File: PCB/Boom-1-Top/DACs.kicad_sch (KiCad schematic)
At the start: 13 parts, among them J36 SPIBus1Test, J37 Osc1Conn, J38 Osc2Conn, U3 AD5290, U4 AD5290

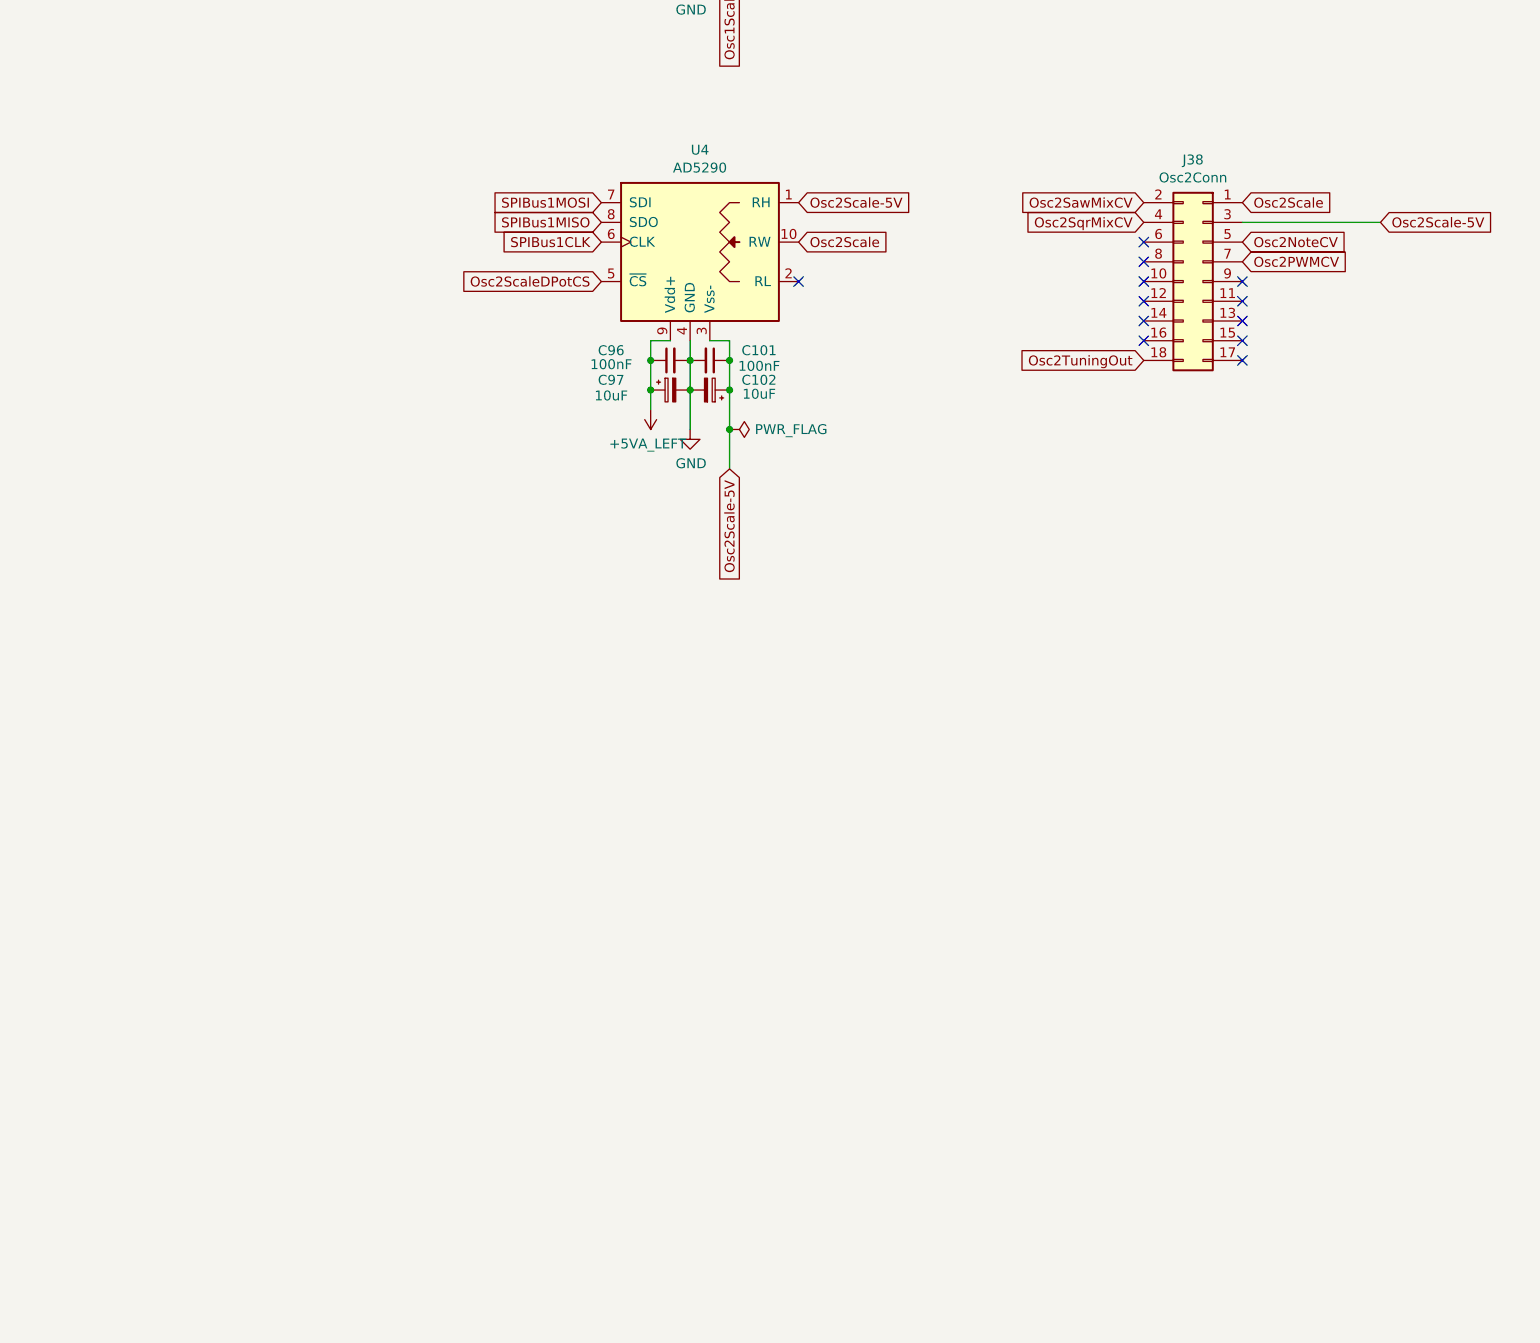
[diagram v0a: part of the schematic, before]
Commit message: Top: moved power connectors to Power Rails; moved anything pertaining to DACs into DACs
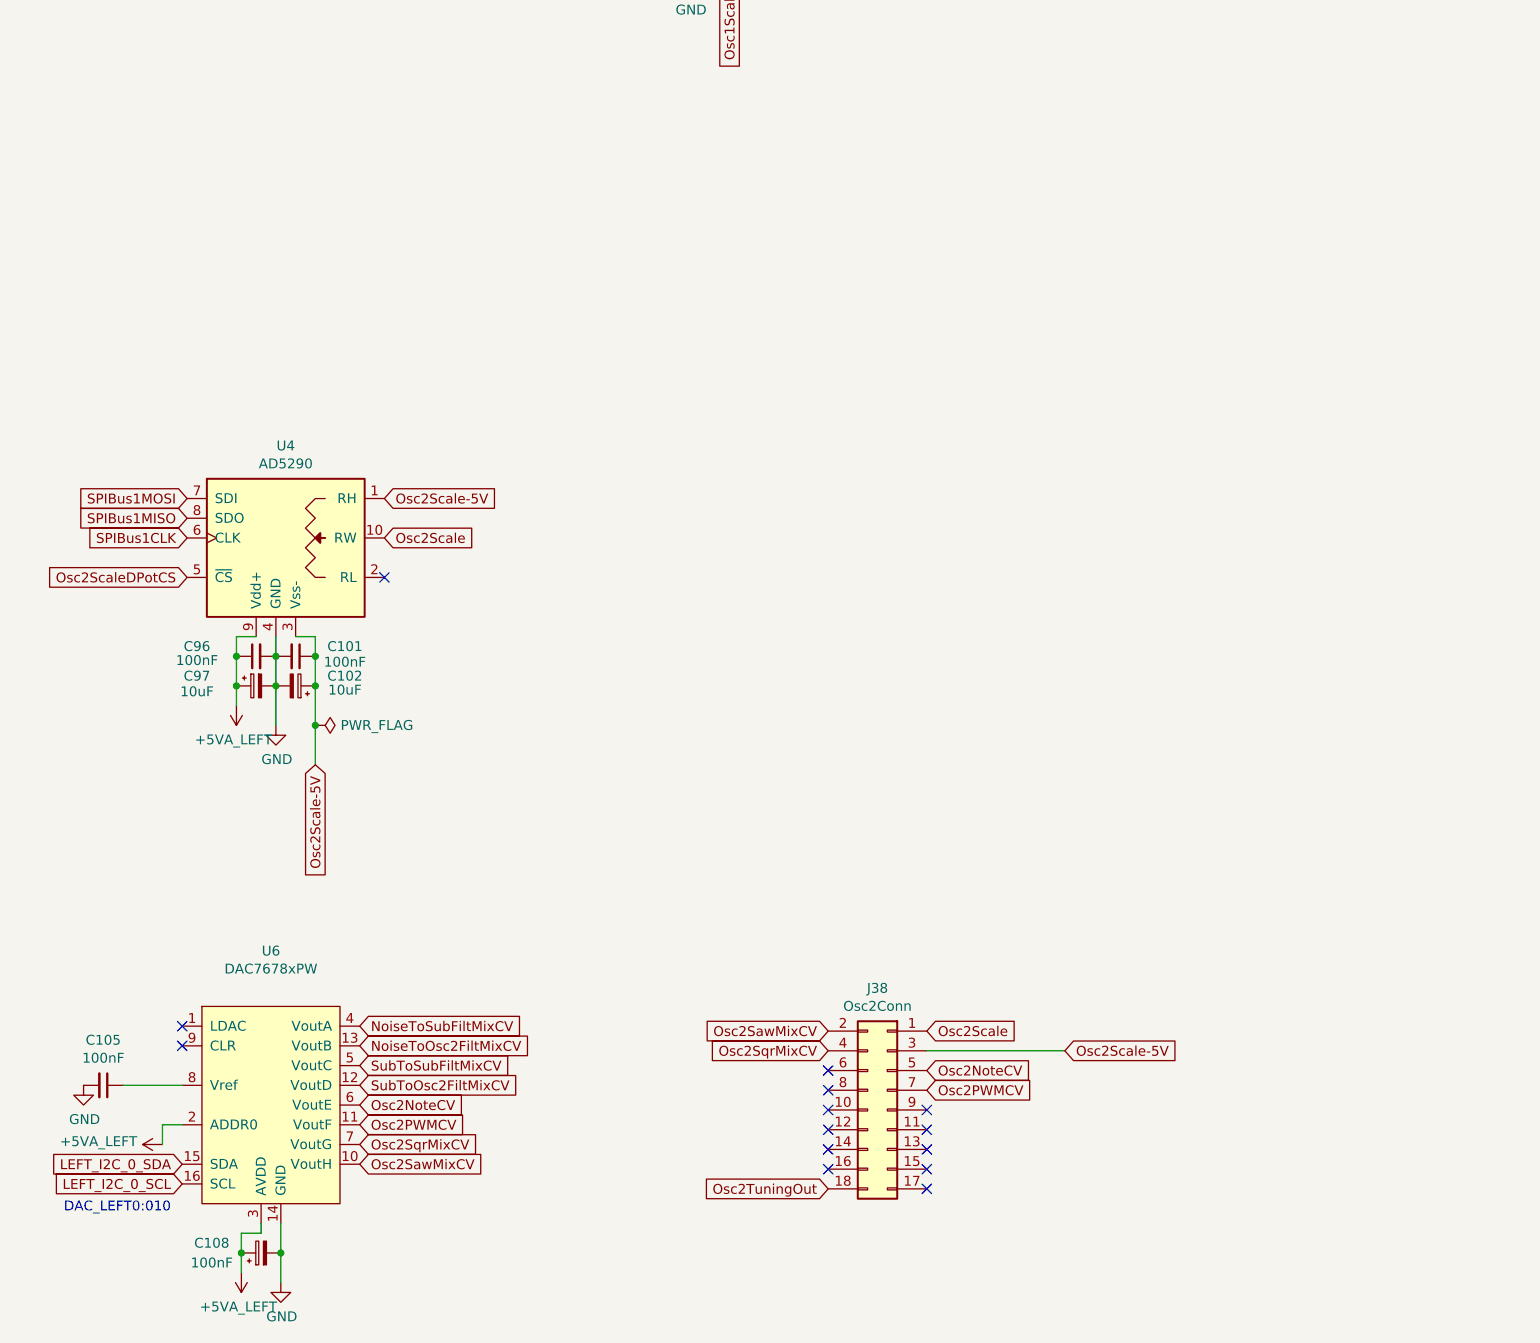
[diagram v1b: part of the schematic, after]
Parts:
- added C105: 100nF, Capacitor_SMD:C_0402_1005Metric, symbol Device:C_Small
- added C108: 100nF, Capacitor_SMD:C_0402_1005Metric, symbol Device:CP_Small
- added U6: DAC7678xPW, Package_SO:TSSOP-16_4.4x5mm_P0.65mm, symbol DAC7678:DAC7678xPW
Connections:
- net +5VA_LEFT: now also C108.1, U6.2 (ADDR0), U6.3 (AVDD)
- net GND: now also C105.2, C108.2, U6.14 (GND)
- net Osc2NoteCV: now also U6.6 (VoutE)
- net Osc2PWMCV: now also U6.11 (VoutF)
- net Osc2SawMixCV: now also U6.10 (VoutH)
- net Osc2SqrMixCV: now also U6.7 (VoutG)
- new net: C105.1, U6.8 (Vref)
- new net LEFT_I2C_0_SCL: U6.16 (SCL)
- new net LEFT_I2C_0_SDA: U6.15 (SDA)
- new net NoiseToOsc2FiltMixCV: U6.13 (VoutB)
- new net NoiseToSubFiltMixCV: U6.4 (VoutA)
- new net SubToOsc2FiltMixCV: U6.12 (VoutD)
- new net SubToSubFiltMixCV: U6.5 (VoutC)
- no-connect marks 22 -> 24
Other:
- note added: "DAC_LEFT0:010"
- moved on the sheet: C101, C102, C96, C97, J38, U4

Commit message: actually moved the DAC-related stuff; DAC page to A1, top-level to A4
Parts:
- added C104, C109, C111, C112, C113, C181, C182, C183, C184, C185, C186, C205, C206, C207, C208, C211, C237, C238: 100nF, Capacitor_SMD:C_0402_1005Metric, symbol Device:C_Small
- added C107, C110, C114, C115, C116, C212: 100nF, Capacitor_SMD:C_0402_1005Metric, symbol Device:CP_Small
- added C189, C190, C191, C192, C193, C194: 560pF, Capacitor_SMD:C_0402_1005Metric, symbol Device:C_Small
- added C197, C198, C199, C200, C201, C202: 100pF, Capacitor_SMD:C_0402_1005Metric, symbol Device:C_Small
- added D10, D8: B5819W, Diode_SMD:D_SOD-123, symbol Device:D_Schottky_Small
- added J24: FiltConn1PassThru, Connector_PinSocket_2.54mm:PinSocket_2x04_P2.54mm_Vertical, symbol Connector_Generic:Conn_02x04_Odd_Even
- added J26: AudioOutConn, Connector_PinSocket_2.54mm:PinSocket_2x02_P2.54mm_Vertical, symbol Connector_Generic:Conn_02x02_Odd_Even
- added J27: FiltConn2PassThru, Connector_PinSocket_2.54mm:PinSocket_1x08_P2.54mm_Vertical, symbol Connector_Generic:Conn_01x08
- added J28: FiltConn2PassThruPower, Connector_PinSocket_2.54mm:PinSocket_1x12_P2.54mm_Vertical, symbol Connector_Generic:Conn_01x12
- added J39: SubNoiseConn, Connector_PinHeader_2.54mm:PinHeader_2x06_P2.54mm_Vertical, symbol Connector_Generic:Conn_02x06_Odd_Even
- added J40: FiltConn2, Connector_PinHeader_2.54mm:PinHeader_2x12_P2.54mm_Vertical, symbol Connector_Generic:Conn_02x12_Odd_Even
- added J41: EnvGenConn2, Connector_PinHeader_2.54mm:PinHeader_2x09_P2.54mm_Vertical, symbol Connector_Generic:Conn_02x09_Odd_Even
- added J42: EnvGenConn1, Connector_PinHeader_2.54mm:PinHeader_2x09_P2.54mm_Vertical, symbol Connector_Generic:Conn_02x09_Odd_Even
- added J43: FXConn1, Connector_PinHeader_2.54mm:PinHeader_2x08_P2.54mm_Vertical, symbol Connector_Generic:Conn_02x08_Odd_Even
- added J44: FiltConn1, Connector_PinHeader_2.54mm:PinHeader_2x04_P2.54mm_Vertical, symbol Connector_Generic:Conn_02x04_Odd_Even
- added J45: FXConn2, Connector_PinHeader_2.54mm:PinHeader_2x05_P2.54mm_Vertical, symbol Connector_Generic:Conn_02x05_Odd_Even
- added J46: EnvGenConn3, Connector_PinHeader_2.54mm:PinHeader_2x09_P2.54mm_Vertical, symbol Connector_Generic:Conn_02x09_Odd_Even
- added R222, R223, R226, R227, R228, R229, R230, R231, R234, R235, R236, R237, R238, R239, R242, R243, R244, R245, R254, R255, R256, R257, R258, R259: 30K, Resistor_SMD:R_0805_2012Metric, symbol Device:R_Small_US
- added R246, R247, R248, R249, R250, R251: 510R, Resistor_SMD:R_0805_2012Metric, symbol Device:R_Small_US
- added R262, R263: 7.5K, Resistor_SMD:R_0805_2012Metric, symbol Device:R_Small_US
- added U10, U5, U50, U7, U8, U9: DAC7678xPW, Package_SO:TSSOP-16_4.4x5mm_P0.65mm, symbol DAC7678:DAC7678xPW
- added U43, U44: V2164D, Package_SO:SOIC-16_3.9x9.9mm_P1.27mm, symbol CustomSymbols:V2164D
- added U45, U46, U47: TL074, Package_SO:SOIC-14_3.9x8.7mm_P1.27mm, symbol Amplifier_Operational:TL074
- added U55, U56: MCP4651, Package_SO:TSSOP-14_4.4x5mm_P0.65mm, symbol MCP4651:MCP4651
- added U57: 24LC32, Package_DIP:DIP-8_W7.62mm_Socket, symbol Memory_EEPROM:24LC32
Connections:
- net +5VA_LEFT: now also C107.1, C110.1, U5.3 (AVDD), U7.3 (AVDD)
- net GND: now also C104.2, C107.2, C109.2, C110.2, C111.2, C112.2, C113.2, C114.2, C115.2, C116.2, C181.2, C182.1, C183.2, C184.1, C185.2, C186.1, C189.2, C190.2, C191.2, C192.2, C193.2, C194.2, C205.1, C206.2, C207.1, C208.2, C211.2, C212.2, C237.1, C238.1, D10.1 (K), D8.1 (K), U10.14 (GND), U43.8 (GND), U44.8 (GND), U45.10 (+), U45.12 (+), U45.3 (+), U45.5 (+), U46.10 (+), U46.12 (+), U46.3 (+), U46.5 (+), U47.10 (+), U47.12 (+), U47.3 (+), U47.5 (+), U5.14 (GND), U5.2 (ADDR0), U50.14 (GND), U55.1 (HVC/A0), U55.12 (A2), U55.13 (A1), U55.14 (VDD), U56.12 (A2), U56.13 (A1), U56.14 (VDD), U56.5 (P1B), U56.7 (P1A), U57.1 (A0), U57.2 (A1), U57.3 (A2), U57.4 (GND), U57.7 (WP), U7.14 (GND), U7.2 (ADDR0), U8.14 (GND), U8.2 (ADDR0), U9.14 (GND)
- net LEFT_I2C_0_SCL: now also U5.16 (SCL), U50.16 (SCL)
- net LEFT_I2C_0_SDA: now also U5.15 (SDA), U50.15 (SDA)
- net NoiseToOsc2FiltMixCV: now also J39.12 (Pin_12)
- net NoiseToSubFiltMixCV: now also J39.10 (Pin_10)
- net Osc1NoteCV: now also U5.5 (VoutC)
- net Osc1PWMCV: now also U5.11 (VoutF)
- net Osc1SawMixCV: now also U5.7 (VoutG)
- net Osc1SqrMixCV: now also U5.10 (VoutH)
- net Osc1ToOsc1FiltMixCV: now also U5.6 (VoutE)
- net Osc1ToOsc2FiltMixCV: now also U5.12 (VoutD)
- net SubToOsc2FiltMixCV: now also J39.1 (Pin_1)
- net SubToSubFiltMixCV: now also J39.9 (Pin_9)
- new net: R236.1, R244.2, U45.8
- new net: R228.1, R236.2, U45.9 (-)
- new net: R235.1, R243.2, U45.7
- new net: R227.1, R235.2, U45.6 (-)
- new net: C189.1, R246.2
- new net: C104.1, U5.8 (Vref)
- new net: C211.1, U50.8 (Vref)
- new net: C112.1, U9.8 (Vref)
- new net: R238.1, R250.1, U44.2 (Ii1)
- new net: R230.1, R238.2, U47.1
- new net: R223.1, R231.2, U47.6 (-)
- new net: R231.1, R239.2, U47.7
- new net: C201.1, R258.2, U44.4 (Io1), U47.9 (-)
- new net: C197.1, R254.2, U43.4 (Io1), U46.2 (-)
- new net: C200.1, R257.2, U43.13 (Io4), U46.13 (-)
- new net: R243.1, R247.1, U43.7 (Ii2)
- new net: C198.1, R255.2, U43.5 (Io2), U46.6 (-)
- new net: R245.1, R249.1, U43.15 (Ii4)
- new net: C192.1, R249.2
- new net: R229.1, R237.2, U45.13 (-)
- new net: R242.1, R246.1, U43.2 (Ii1)
- new net: C113.1, U10.8 (Vref)
- new net: R239.1, R251.1, U44.7 (Ii2)
- new net: C194.1, R251.2
- new net: R237.1, R245.2, U45.14
- new net: R263.1, U44.1 (Mode)
- new net: R234.1, R242.2, U45.1
- new net: R262.1, U43.1 (Mode)
- new net: C193.1, R250.2
- new net: R244.1, R248.1, U43.10 (Ii3)
- new net: C191.1, R248.2
- new net: C202.1, R259.2, U44.5 (Io2), U47.13 (-)
- new net: R222.1, R230.2, U47.2 (-)
- new net: C109.1, U7.8 (Vref)
- new net: C111.1, U8.8 (Vref)
- new net: R226.1, R234.2, U45.2 (-)
- new net: C199.1, R256.2, U43.12 (Io3), U46.9 (-)
- new net: C190.1, R247.2
- new net +12VA: C181.1, C183.1, C185.1, C205.2, C207.2, R262.2, R263.2, U43.16 (V+), U44.16 (V+), U45.4 (V+), U46.4 (V+), U47.4 (V+)
- new net +3V3: C237.2, C238.2, U55.4 (VSS), U56.1 (HVC/A0), U56.4 (VSS), U57.8 (VCC)
- new net +5VA_RIGHT: C114.1, C115.1, C116.1, U10.3 (AVDD), U8.3 (AVDD), U9.2 (ADDR0), U9.3 (AVDD)
- new net +5VA_TOP: C212.1, U50.3 (AVDD)
- new net -12VA: C182.2, C184.2, C186.2, C206.1, C208.1, D10.2 (A), D8.2 (A), U43.9 (V-), U44.9 (V-), U45.11 (V-), U46.11 (V-), U47.11 (V-)
- new net FV1Ctrl1Wiper: J43.3 (Pin_3), U55.9 (P0W)
- new net FV1Ctrl2Wiper: J43.5 (Pin_5), U55.6 (P1W)
- new net FV1Ctrl3Wiper: J43.7 (Pin_7), U56.9 (P0W)
- new net FV1CtrlHigh: J43.1 (Pin_1), U55.10 (P0B), U55.5 (P1B), U56.10 (P0B)
- new net FV1CtrlLow: J43.10 (Pin_10), J43.11 (Pin_11), J43.12 (Pin_12), J43.13 (Pin_13), J43.14 (Pin_14), J43.15 (Pin_15), J43.16 (Pin_16), J43.2 (Pin_2), J43.4 (Pin_4), J43.6 (Pin_6), J43.8 (Pin_8), J43.9 (Pin_9), U55.7 (P1A), U55.8 (P0A), U56.8 (P0A)
- new net FV1EEpromSCL: J45.5 (Pin_5), U57.6 (SCL)
- new net FV1EEpromSDA: J45.7 (Pin_7), U57.5 (SDA)
- new net FV1FeedbackCV: J45.2 (Pin_2), U50.10 (VoutH)
- new net FV1WetDryCV: J45.4 (Pin_4), U50.7 (VoutG)
- new net FiltConn1+12V: J24.1 (Pin_1), J44.1 (Pin_1)
- new net FiltConn1-12V: J24.5 (Pin_5), J44.5 (Pin_5)
- new net FiltConn1-GND: J24.3 (Pin_3), J24.7 (Pin_7), J44.7 (Pin_7)
- new net FiltConn2+12V: J28.12 (Pin_12), J28.3 (Pin_3), J28.6 (Pin_6), J28.9 (Pin_9), J40.14 (Pin_14), J40.2 (Pin_2)
- new net FiltConn2-12V: J28.11 (Pin_11), J28.2 (Pin_2), J28.5 (Pin_5), J28.8 (Pin_8), J40.6 (Pin_6)
- new net FiltConn2GND: J28.1 (Pin_1), J28.10 (Pin_10), J28.4 (Pin_4), J28.7 (Pin_7), J40.10 (Pin_10), J40.4 (Pin_4)
- new net LEFT_I2C_2_SCL: U55.2 (SCL), U56.2 (SCL), U7.16 (SCL)
- new net LEFT_I2C_2_SDA: U55.3 (SDA), U56.3 (SDA), U7.15 (SDA)
- new net MixOutGND: J26.2 (Pin_2), J26.4 (Pin_4), J45.10 (Pin_10)
- new net MixOutLeftTip: J26.1 (Pin_1), J45.6 (Pin_6)
- new net MixOutRightTip: J26.3 (Pin_3), J45.8 (Pin_8)
- new net Osc1FXReturn: J24.8 (Pin_8), J44.8 (Pin_8)
- new net Osc1FXSend: J24.2 (Pin_2), J44.2 (Pin_2)
- new net Osc1FiltFreqCV: J44.4 (Pin_4), U5.13 (VoutB)
- new net Osc1FiltResCV: J44.6 (Pin_6), U5.4 (VoutA)
- new net Osc2FXReturn: J27.1 (Pin_1), J40.3 (Pin_3)
- new net Osc2FXSend: J27.2 (Pin_2), J40.7 (Pin_7)
- new net Osc2FiltFreqCV: J40.1 (Pin_1), U7.11 (VoutF)
- new net Osc2FiltResCV: J40.5 (Pin_5), U7.4 (VoutA)
- new net OscAmpEnvAmtCV: U43.11 (Vc3), U50.5 (VoutC)
- new net OscAmpEnvAmtHigh: J41.5 (Pin_5), R228.2
- new net OscAmpEnvAmtWiper: C199.2, J41.7 (Pin_7), R256.1, U46.8
- new net OscAmpEnvAttackCV: J41.8 (Pin_8), U9.6 (VoutE)
- new net OscAmpEnvDecayCV: J41.6 (Pin_6), U9.7 (VoutG)
- new net OscAmpEnvGate: J41.3 (Pin_3)
- new net OscAmpEnvReleaseCV: J41.2 (Pin_2), U9.4 (VoutA)
- new net OscAmpEnvSustainCV: J41.4 (Pin_4), U9.5 (VoutC)
- new net OscAmpEnvTrigger: J41.1 (Pin_1)
- new net OscFiltEnv1AmtCV: U43.3 (Vc1), U50.4 (VoutA)
- new net OscFiltEnv1AmtHigh: J42.5 (Pin_5), R226.2
- new net OscFiltEnv1AmtWiper: C197.2, J42.7 (Pin_7), R254.1, U46.1
- new net OscFiltEnv1AttackCV: J42.8 (Pin_8), U8.6 (VoutE)
- new net OscFiltEnv1DecayCV: J42.6 (Pin_6), U8.7 (VoutG)
- new net OscFiltEnv1Gate: J42.3 (Pin_3)
- new net OscFiltEnv1ReleaseCV: J42.2 (Pin_2), U8.4 (VoutA)
- new net OscFiltEnv1SustainCV: J42.4 (Pin_4), U8.5 (VoutC)
- new net OscFiltEnv1Trigger: J42.1 (Pin_1)
- new net OscFiltEnv2AmtCV: U43.6 (Vc2), U50.13 (VoutB)
- new net OscFiltEnv2AmtHigh: J42.12 (Pin_12), R227.2
- new net OscFiltEnv2AmtWiper: C198.2, J42.10 (Pin_10), R255.1, U46.7
- new net OscFiltEnv2AttackCV: J42.9 (Pin_9), U8.10 (VoutH)
- new net OscFiltEnv2DecayCV: J42.11 (Pin_11), U8.11 (VoutF)
- new net OscFiltEnv2Gate: J42.14 (Pin_14)
- new net OscFiltEnv2ReleaseCV: J42.15 (Pin_15), U8.13 (VoutB)
- new net OscFiltEnv2SustainCV: J42.13 (Pin_13), U8.12 (VoutD)
- new net OscFiltEnv2Trigger: J42.16 (Pin_16)
- new net PreFV1FXReturn: J27.6 (Pin_6), J40.19 (Pin_19)
- new net PreFV1FXSend: J27.5 (Pin_5), J40.17 (Pin_17)
- new net RIGHT_I2C_2_SCL: U10.16 (SCL), U8.16 (SCL), U9.16 (SCL)
- new net RIGHT_I2C_2_SDA: U10.15 (SDA), U8.15 (SDA), U9.15 (SDA)
- new net SubAmpAudioBypassReturn: J27.7 (Pin_7), J40.20 (Pin_20)
- new net SubAmpAudioBypassSend: J27.8 (Pin_8), J40.22 (Pin_22)
- new net SubAmpEnvAmtCV: U43.14 (Vc4), U50.12 (VoutD)
- new net SubAmpEnvAmtHigh: J41.12 (Pin_12), R229.2
- new net SubAmpEnvAmtWiper: C200.2, J41.10 (Pin_10), R257.1, U46.14
- new net SubAmpEnvAttackCV: J41.9 (Pin_9), U9.10 (VoutH)
- new net SubAmpEnvDecayCV: J41.11 (Pin_11), U9.11 (VoutF)
- new net SubAmpEnvGate: J41.14 (Pin_14)
- new net SubAmpEnvReleaseCV: J41.15 (Pin_15), U9.13 (VoutB)
- new net SubAmpEnvSustainCV: J41.13 (Pin_13), U9.12 (VoutD)
- new net SubAmpEnvTrigger: J41.16 (Pin_16)
- new net SubFXReturn: J27.3 (Pin_3), J40.11 (Pin_11)
- new net SubFXSend: J27.4 (Pin_4), J40.13 (Pin_13)
- new net SubFiltEnv1AmtCV: U44.6 (Vc2), U50.11 (VoutF)
- new net SubFiltEnv1AmtHigh: J46.12 (Pin_12), R223.2
- new net SubFiltEnv1AmtWiper: C202.2, J46.10 (Pin_10), R259.1, U47.14
- new net SubFiltEnv1AttackCV: J46.9 (Pin_9), U10.10 (VoutH)
- new net SubFiltEnv1DecayCV: J46.11 (Pin_11), U10.11 (VoutF)
- new net SubFiltEnv1Gate: J46.14 (Pin_14)
- new net SubFiltEnv1ReleaseCV: J46.15 (Pin_15), U10.13 (VoutB)
- new net SubFiltEnv1SustainCV: J46.13 (Pin_13), U10.12 (VoutD)
- new net SubFiltEnv1Trigger: J46.16 (Pin_16)
- new net SubFiltEnv2AmtCV: U44.3 (Vc1), U50.6 (VoutE)
- new net SubFiltEnv2AmtHigh: J46.7 (Pin_7), R222.2
- new net SubFiltEnv2AmtWiper: C201.2, J46.5 (Pin_5), R258.1, U47.8
- new net SubFiltEnv2AttackCV: J46.8 (Pin_8), U10.6 (VoutE)
- new net SubFiltEnv2DecayCV: J46.6 (Pin_6), U10.7 (VoutG)
- new net SubFiltEnv2Gate: J46.3 (Pin_3)
- new net SubFiltEnv2ReleaseCV: J46.2 (Pin_2), U10.4 (VoutA)
- new net SubFiltEnv2SustainCV: J46.4 (Pin_4), U10.5 (VoutC)
- new net SubFiltEnv2Trigger: J46.1 (Pin_1)
- new net SubFiltFreqCV: J40.9 (Pin_9), U7.5 (VoutC)
- new net SubFiltResCV: J40.15 (Pin_15), U7.6 (VoutE)
- no-connect marks 24 -> 76
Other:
- note added: "DAC_LEFT0:000"
- note added: "DAC_LEFT0:100"
- note added: "DAC_LEFT2:000"
- note added: "DAC_RIGHT2:000"
- note added: "DAC_RIGHT2:010"
- note added: "DAC_RIGHT2:100"

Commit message: VCA subsheet
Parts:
- removed C181, C182, C183, C184, C185, C186, C205, C206, C207, C208, C211: 100nF, Capacitor_SMD:C_0402_1005Metric, symbol Device:C_Small
- removed C189, C190, C191, C192, C193, C194: 560pF, Capacitor_SMD:C_0402_1005Metric, symbol Device:C_Small
- removed C197, C198, C199, C200, C201, C202: 100pF, Capacitor_SMD:C_0402_1005Metric, symbol Device:C_Small
- removed C212: 100nF, Capacitor_SMD:C_0402_1005Metric, symbol Device:CP_Small
- removed D10, D8: B5819W, Diode_SMD:D_SOD-123, symbol Device:D_Schottky_Small
- removed J45: FXConn2, Connector_PinHeader_2.54mm:PinHeader_2x05_P2.54mm_Vertical, symbol Connector_Generic:Conn_02x05_Odd_Even
- removed R222, R223, R226, R227, R228, R229, R230, R231, R234, R235, R236, R237, R238, R239, R242, R243, R244, R245, R254, R255, R256, R257, R258, R259: 30K, Resistor_SMD:R_0805_2012Metric, symbol Device:R_Small_US
- removed R246, R247, R248, R249, R250, R251: 510R, Resistor_SMD:R_0805_2012Metric, symbol Device:R_Small_US
- removed R262, R263: 7.5K, Resistor_SMD:R_0805_2012Metric, symbol Device:R_Small_US
- removed U43, U44: V2164D, Package_SO:SOIC-16_3.9x9.9mm_P1.27mm, symbol CustomSymbols:V2164D
- removed U45, U46, U47: TL074, Package_SO:SOIC-14_3.9x8.7mm_P1.27mm, symbol Amplifier_Operational:TL074
- removed U50: DAC7678xPW, Package_SO:TSSOP-16_4.4x5mm_P0.65mm, symbol DAC7678:DAC7678xPW
- removed U57: 24LC32, Package_DIP:DIP-8_W7.62mm_Socket, symbol Memory_EEPROM:24LC32
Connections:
- no-connect marks 76 -> 64
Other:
- added sheet VCA Control (VCA_Control.kicad_sch)
- note removed: "DAC_LEFT0:100"
- moved on the sheet: C104, C105, C107, C108, C109, C110, C111, C112, C113, C114, C115, C116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
